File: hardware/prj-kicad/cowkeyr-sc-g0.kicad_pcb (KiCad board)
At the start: 2 copper layers, 80 x 60 mm, 0 parts

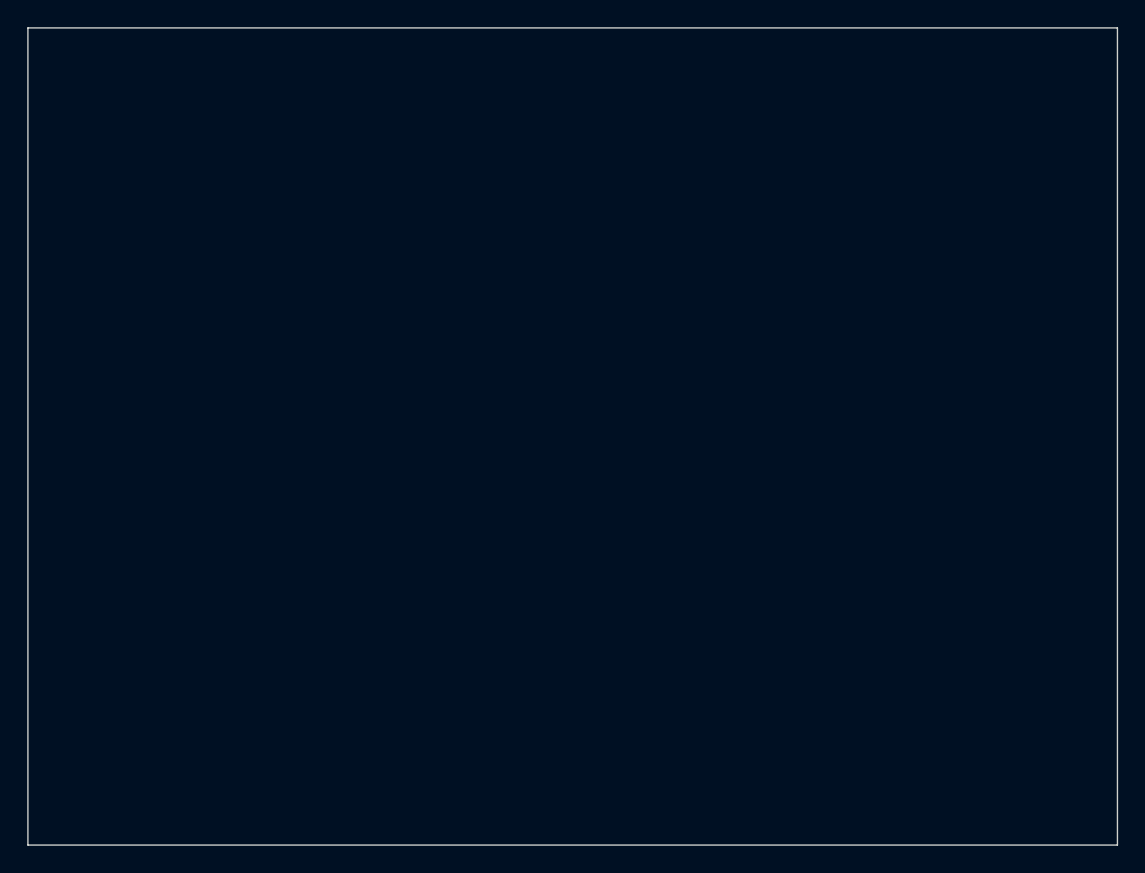
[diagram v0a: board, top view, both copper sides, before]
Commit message: HW: Insert SmartCard connector (sch + footprint)
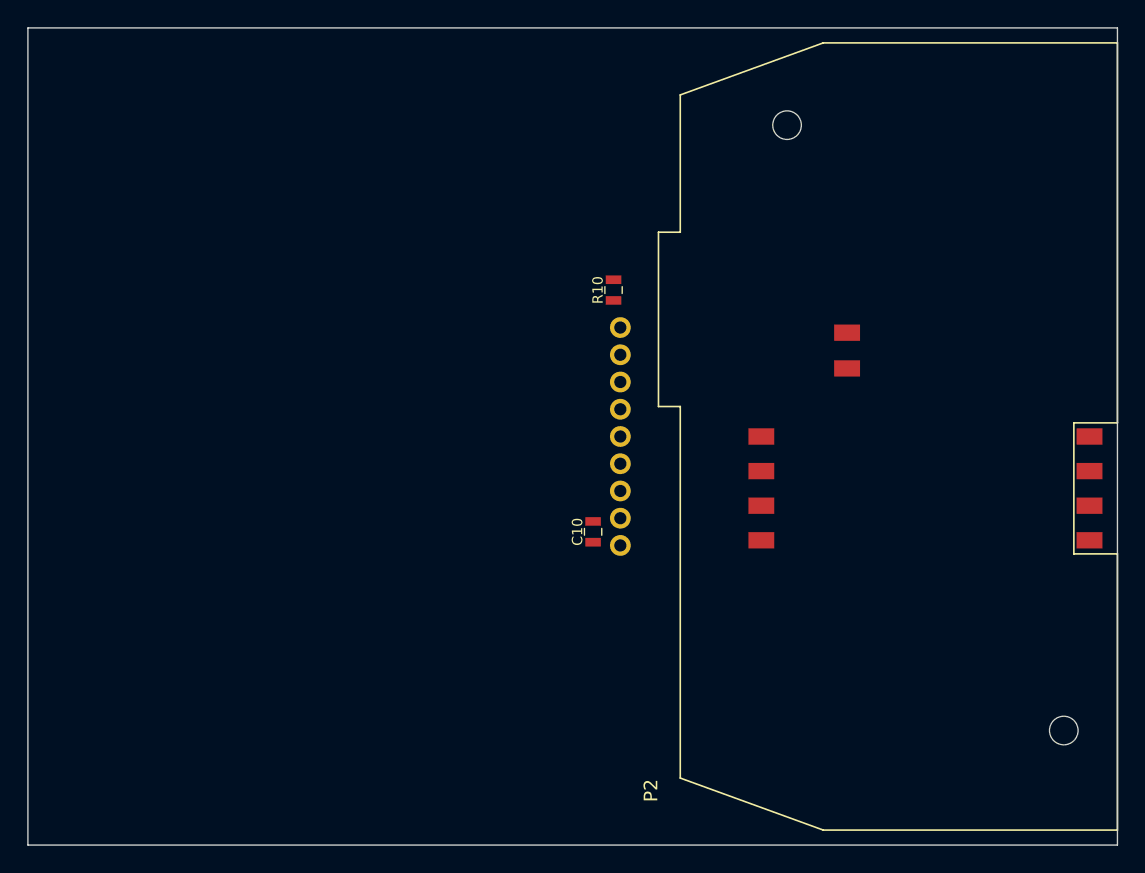
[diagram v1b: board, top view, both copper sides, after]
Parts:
- added C10: 1uF, cowkeyr-sc-g0:SMD0603, F.Cu at (150.0, 112.0)
- added P2: CONN_SC, cowkeyr-sc-g0:CONN_7312P0225AxxLF, F.Cu at (174.4, 105.0)
- added R10: 10k, cowkeyr-sc-g0:SMD0603, F.Cu at (151.5, 94.2)
- added TP_SC0: CONN_1, cowkeyr-sc-g0:TP_PIN, F.Cu at (152.0, 97.0)
- added TP_SC1: CONN_1, cowkeyr-sc-g0:TP_PIN, F.Cu at (152.0, 113.0)
- added TP_SC2: CONN_1, cowkeyr-sc-g0:TP_PIN, F.Cu at (152.0, 109.0)
- added TP_SC3: CONN_1, cowkeyr-sc-g0:TP_PIN, F.Cu at (152.0, 105.0)
- added TP_SC4: CONN_1, cowkeyr-sc-g0:TP_PIN, F.Cu at (152.0, 103.0)
- added TP_SC5: CONN_1, cowkeyr-sc-g0:TP_PIN, F.Cu at (152.0, 111.0)
- added TP_SC6: CONN_1, cowkeyr-sc-g0:TP_PIN, F.Cu at (152.0, 107.0)
- added TP_SC7: CONN_1, cowkeyr-sc-g0:TP_PIN, F.Cu at (152.0, 101.0)
- added TP_SC8: CONN_1, cowkeyr-sc-g0:TP_PIN, F.Cu at (152.0, 99.0)
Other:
- board text removed: "Smartcard connector"

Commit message: HW: Replace smartcard connector (bad size) and add power supplies
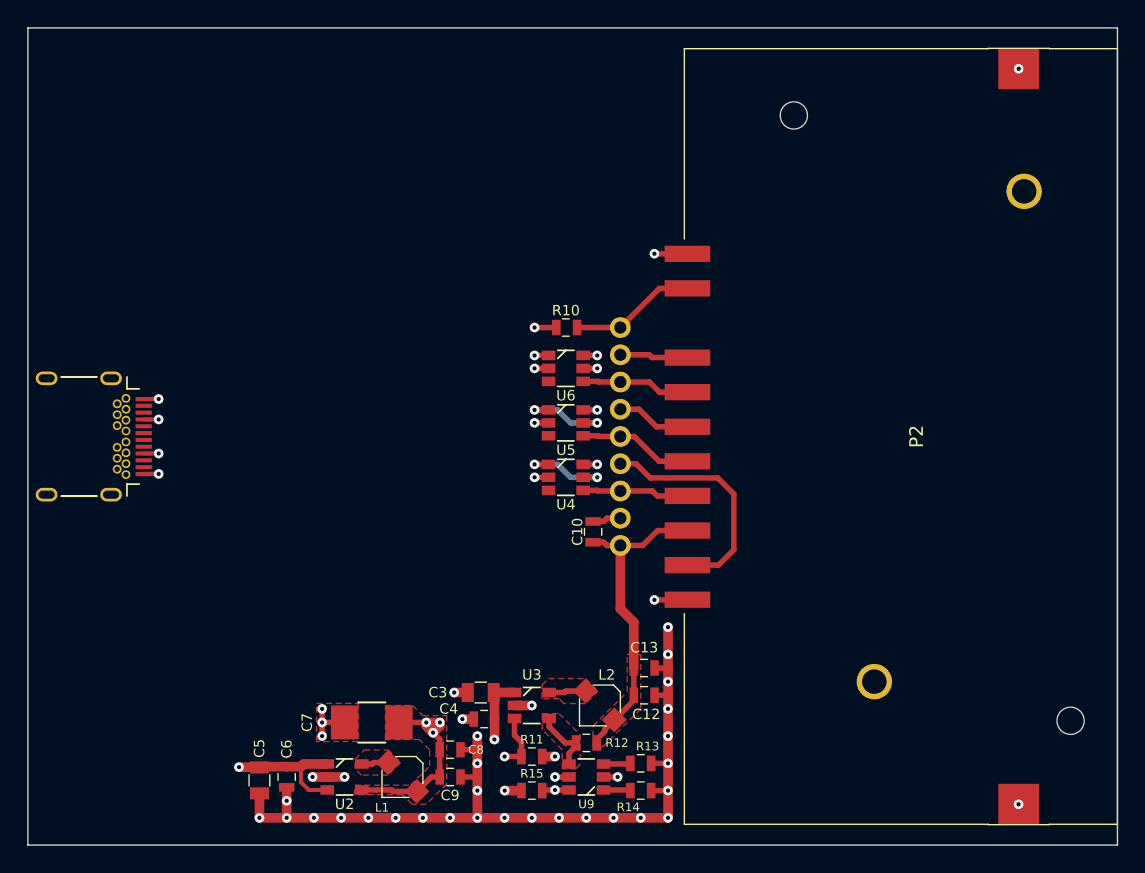
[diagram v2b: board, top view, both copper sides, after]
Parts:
- added C12: 4,7uF, cowkeyr-sc-g0:SMD0603, F.Cu at (153.8, 124.0)
- added C13: 4,7uF, cowkeyr-sc-g0:SMD0603, F.Cu at (153.8, 122.0)
- added C3: 10uF, cowkeyr-sc-g0:SMD0805, F.Cu at (141.8, 123.8)
- added C4: 100nF, cowkeyr-sc-g0:SMD0603, F.Cu at (142.0, 125.8)
- added C5: 10uF, cowkeyr-sc-g0:SMD0805, F.Cu at (125.5, 130.2)
- added C6: 470pF, cowkeyr-sc-g0:SMD0603, F.Cu at (127.5, 130.0)
- added C7: n/a, cowkeyr-sc-g0:SMD1210, F.Cu at (133.8, 126.0)
- added C8: 4,7uF, cowkeyr-sc-g0:SMD0603, F.Cu at (139.5, 128.0)
- added C9: 4,7uF, cowkeyr-sc-g0:SMD0603, F.Cu at (139.5, 130.0)
- added L1: 2,2uH, cowkeyr-sc-g0:I_CDRH2D14, F.Cu at (136.0, 130.0)
- added L2: 2,2uH, cowkeyr-sc-g0:I_CDRH2D14, F.Cu at (150.5, 124.8)
- added P1: CONN_USB-C, cowkeyr-sc-g0:CONN_632723300011, F.Cu at (115.1, 105.0)
- added R11: 10k, cowkeyr-sc-g0:SMD0603, F.Cu at (145.5, 128.5)
- added R12: 422k, cowkeyr-sc-g0:SMD0603, F.Cu at (149.5, 127.5)
- added R13: 75k, cowkeyr-sc-g0:SMD0603, F.Cu at (153.5, 129.0)
- added R14: 47k, cowkeyr-sc-g0:SMD0603, F.Cu at (153.5, 131.0)
- added R15: 10k, cowkeyr-sc-g0:SMD0603, F.Cu at (145.5, 131.0)
- added U2: LM3671, cowkeyr-sc-g0:SOT23-5, F.Cu at (131.8, 130.0)
- added U3: LM3671, cowkeyr-sc-g0:SOT23-5, F.Cu at (145.5, 124.8)
- added U4: SN74LVC1T45, cowkeyr-sc-g0:SOT23-6, F.Cu at (148.0, 108.0)
- added U5: SN74LVC1T45, cowkeyr-sc-g0:SOT23-6, F.Cu at (148.0, 104.0)
- added U6: SN74LVC1T45, cowkeyr-sc-g0:SOT23-6, F.Cu at (148.0, 100.0)
- added U9: SN74LVC1G3157, cowkeyr-sc-g0:SOT23-6, F.Cu at (149.5, 130.0)
- P2: footprint cowkeyr-sc-g0:CONN_7312P0225AxxLF -> cowkeyr-sc-g0:CONN_CCM01-25xx
- moved R10 4.45 mm to (148.0, 97.0), turned to 180 degrees
- moved P2 0.15 mm to (174.2, 105.0)
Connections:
- net SC_CLK renamed SC_RAW_CLK
- net SC_IO renamed SC_RAW_IO
- net SC_RST renamed SC_RAW_RST
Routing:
- net GND: track 0.00 -> 276.8 mm, vias 0 -> 47
- net +3.3V: track 0.00 -> 80.9 mm, vias 0 -> 10
- net +VBus: track 0.00 -> 78.2 mm, vias 0 -> 4
- net +V_SC: track 0.00 -> 43.9 mm, vias 0 -> 3
- net SC_C6: track 0.00 -> 17.2 mm
- net SC_DETECT: track 0.00 -> 9.29 mm
- net SC_RAW_CLK: track 0.00 -> 8.43 mm
- net SC_RAW_IO: track 0.00 -> 7.98 mm
- net SC_RAW_RST: track 0.00 -> 7.83 mm
- net SC_C4: track 0.00 -> 5.46 mm
- net SC_C8: track 0.00 -> 5.01 mm
- net /SC_FB: track 0.00 -> 4.83 mm
- net SC_PWR_EN: track 0.00 -> 4.25 mm, vias 0 -> 1
- net /SC_SW: track 0.00 -> 2.71 mm
- net SC_PWR_SEL: track 0.00 -> 1.99 mm, vias 0 -> 1
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- added copper zone on F.Cu, net +3.3V
- added copper zone on F.Cu, net +V_SC
- added copper zone on F.Cu, net /SC_FB
- added copper zone on F.Cu, net /SC_SW
- added copper zone on F.Cu, net /V_SW
- added copper zone on F.Cu, net GND
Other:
- copper layers 2 -> 4
